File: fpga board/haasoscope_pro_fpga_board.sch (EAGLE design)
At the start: 406 parts, among them IC1 EP4CE30F23C6N, IC2 EPCQ16ASI8N, J1 2x5, SW1 SKQGADE010, SW2 SKQGADE010, U1 AMS1117-3.3, U2 AMS1117-2.5, U3 AMS1117-1.2, Y1 OSCILLATORSMD-5X3

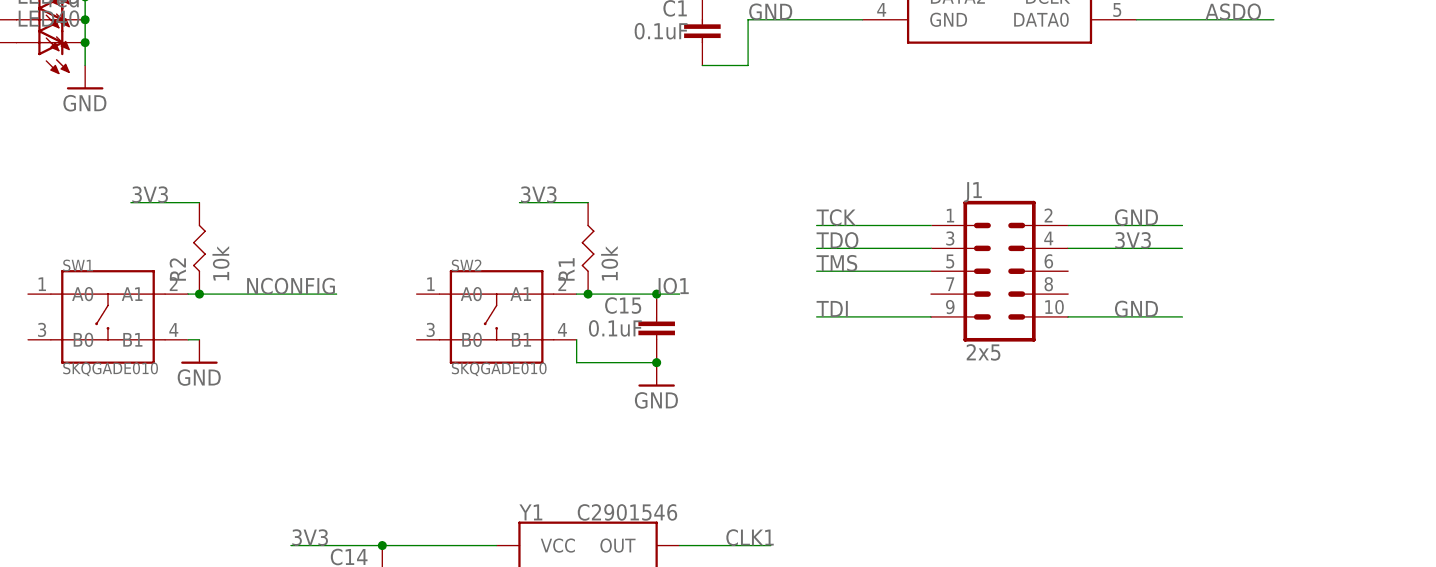
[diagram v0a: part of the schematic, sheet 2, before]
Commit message: pull tms and tdi up to 3v3
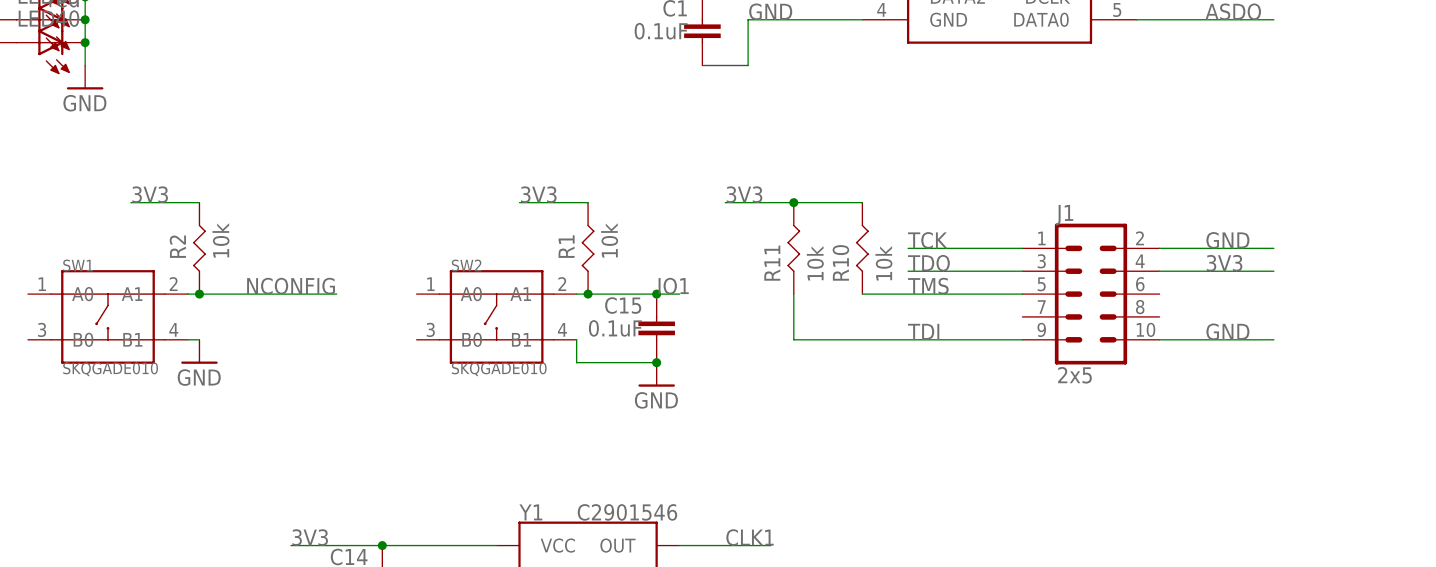
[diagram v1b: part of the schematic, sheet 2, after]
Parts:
- added R10, R11: 10k, FlashPCB_Resistors:RES-0402
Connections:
- net 3V3: now also R10.P$2, R11.P$2
- net TDI: now also R11.P$1
- net TMS: now also R10.P$1
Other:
- moved on the sheet: J1
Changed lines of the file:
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@@
 <part name="JP341" library="pinhead" library_urn="urn:adsk.eagle:library:325" deviceset="PINHD-1X1" device="" package3d_urn="urn:adsk.eagle:package:22485/2" value="1"/>
 <part name="JP342" library="pinhead" library_urn="urn:adsk.eagle:library:325" deviceset="PINHD-1X1" device="" package3d_urn="urn:adsk.eagle:package:22485/2" value="1"/>
+<part name="R10" library="FlashPCB_Resistors" deviceset="RES-0402" device="" value="10k"/>
+<part name="R11" library="FlashPCB_Resistors" deviceset="RES-0402" device="" value="10k"/>
 </parts>
 <sheets>
@@
 <attribute name="VALUE" x="92.456" y="197.739" size="1.778" layer="96" rot="R180"/>
 </instance>
-<instance part="J1" gate="G$1" x="127" y="170.18" smashed="yes">
-<attribute name="VALUE" x="123.19" y="160.274" size="1.778" layer="96" font="vector"/>
-<attribute name="NAME" x="123.19" y="178.308" size="1.778" layer="95" font="vector"/>
+<instance part="J1" gate="G$1" x="137.16" y="167.64" smashed="yes">
+<attribute name="VALUE" x="133.35" y="157.734" size="1.778" layer="96" font="vector"/>
+<attribute name="NAME" x="133.35" y="175.768" size="1.778" layer="95" font="vector"/>
 </instance>
 <instance part="C14" gate="C$1" x="58.42" y="134.62" smashed="yes" rot="R180">
@@
 </instance>
 <instance part="R1" gate="G$1" x="81.28" y="172.72" smashed="yes" rot="R90">
-<attribute name="NAME" x="79.7814" y="168.91" size="1.778" layer="95" rot="R90"/>
-<attribute name="VALUE" x="84.582" y="168.91" size="1.778" layer="96" rot="R90"/>
+<attribute name="NAME" x="79.7814" y="171.45" size="1.778" layer="95" rot="R90"/>
+<attribute name="VALUE" x="84.582" y="171.45" size="1.778" layer="96" rot="R90"/>
 </instance>
 <instance part="C15" gate="C$1" x="88.9" y="162.56" smashed="yes" rot="R180">
@@
 </instance>
 <instance part="R2" gate="G$1" x="38.1" y="172.72" smashed="yes" rot="R90">
-<attribute name="NAME" x="36.6014" y="168.91" size="1.778" layer="95" rot="R90"/>
-<attribute name="VALUE" x="41.402" y="168.91" size="1.778" layer="96" rot="R90"/>
+<attribute name="NAME" x="36.6014" y="171.45" size="1.778" layer="95" rot="R90"/>
+<attribute name="VALUE" x="41.402" y="171.45" size="1.778" layer="96" rot="R90"/>
 </instance>
 <instance part="R3" gate="G$1" x="7.62" y="170.18" smashed="yes" rot="R90">
@@
 <attribute name="VALUE" x="48.26" y="-10.16" size="1.778" layer="96"/>
 </instance>
+<instance part="R10" gate="G$1" x="111.76" y="172.72" smashed="yes" rot="R90">
+<attribute name="NAME" x="110.2614" y="168.91" size="1.778" layer="95" rot="R90"/>
+<attribute name="VALUE" x="115.062" y="168.91" size="1.778" layer="96" rot="R90"/>
+</instance>
+<instance part="R11" gate="G$1" x="104.14" y="172.72" smashed="yes" rot="R90">
+<attribute name="NAME" x="102.6414" y="168.91" size="1.778" layer="95" rot="R90"/>
+<attribute name="VALUE" x="107.442" y="168.91" size="1.778" layer="96" rot="R90"/>
+</instance>
 </instances>
 <busses>
@@
 <segment>
 <pinref part="J1" gate="G$1" pin="2"/>
-<wire x1="134.62" y1="175.26" x2="147.32" y2="175.26" width="0.1524" layer="91"/>
-<label x="139.7" y="175.26" size="1.778" layer="95"/>
+<wire x1="144.78" y1="172.72" x2="157.48" y2="172.72" width="0.1524" layer="91"/>
+<label x="149.86" y="172.72" size="1.778" layer="95"/>
 </segment>
 <segment>
 <pinref part="J1" gate="G$1" pin="10"/>
-<wire x1="134.62" y1="165.1" x2="147.32" y2="165.1" width="0.1524" layer="91"/>
-<label x="139.7" y="165.1" size="1.778" layer="95"/>
+<wire x1="144.78" y1="162.56" x2="157.48" y2="162.56" width="0.1524" layer="91"/>
+<label x="149.86" y="162.56" size="1.778" layer="95"/>
 </segment>
 <segment>
@@
 <segment>
 <pinref part="J1" gate="G$1" pin="4"/>
-<wire x1="134.62" y1="172.72" x2="147.32" y2="172.72" width="0.1524" layer="91"/>
-<label x="139.7" y="172.72" size="1.778" layer="95"/>
+<wire x1="144.78" y1="170.18" x2="157.48" y2="170.18" width="0.1524" layer="91"/>
+<label x="149.86" y="170.18" size="1.778" layer="95"/>
 </segment>
 <segment>
@@
 <label x="111.76" y="101.6" size="1.778" layer="95"/>
 </segment>
+<segment>
+<pinref part="R10" gate="G$1" pin="P$2"/>
+<wire x1="111.76" y1="177.8" x2="104.14" y2="177.8" width="0.1524" layer="91"/>
+<pinref part="R11" gate="G$1" pin="P$2"/>
+<junction x="104.14" y="177.8"/>
+<label x="96.52" y="177.8" size="1.778" layer="95"/>
+<wire x1="96.52" y1="177.8" x2="104.14" y2="177.8" width="0.1524" layer="91"/>
+</segment>
 </net>
 <net name="N$33" class="0">
@@
 <segment>
 <pinref part="J1" gate="G$1" pin="5"/>
-<wire x1="119.38" y1="170.18" x2="106.68" y2="170.18" width="0.1524" layer="91"/>
-<label x="106.68" y="170.18" size="1.778" layer="95"/>
+<wire x1="129.54" y1="167.64" x2="111.76" y2="167.64" width="0.1524" layer="91"/>
+<label x="116.84" y="167.64" size="1.778" layer="95"/>
+<pinref part="R10" gate="G$1" pin="P$1"/>
 </segment>
 </net>
@@
 <segment>
 <pinref part="J1" gate="G$1" pin="1"/>
-<wire x1="119.38" y1="175.26" x2="106.68" y2="175.26" width="0.1524" layer="91"/>
-<label x="106.68" y="175.26" size="1.778" layer="95"/>
+<wire x1="129.54" y1="172.72" x2="116.84" y2="172.72" width="0.1524" layer="91"/>
+<label x="116.84" y="172.72" size="1.778" layer="95"/>
 </segment>
 </net>
@@
 <segment>
 <pinref part="J1" gate="G$1" pin="3"/>
-<wire x1="119.38" y1="172.72" x2="106.68" y2="172.72" width="0.1524" layer="91"/>
-<label x="106.68" y="172.72" size="1.778" layer="95"/>
+<wire x1="129.54" y1="170.18" x2="116.84" y2="170.18" width="0.1524" layer="91"/>
+<label x="116.84" y="170.18" size="1.778" layer="95"/>
 </segment>
 </net>
@@
 <segment>
 <pinref part="J1" gate="G$1" pin="9"/>
-<wire x1="119.38" y1="165.1" x2="106.68" y2="165.1" width="0.1524" layer="91"/>
-<label x="106.68" y="165.1" size="1.778" layer="95"/>
+<label x="116.84" y="162.56" size="1.778" layer="95"/>
+<pinref part="R11" gate="G$1" pin="P$1"/>
+<wire x1="104.14" y1="167.64" x2="104.14" y2="162.56" width="0.1524" layer="91"/>
+<wire x1="104.14" y1="162.56" x2="129.54" y2="162.56" width="0.1524" layer="91"/>
 </segment>
 </net>

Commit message: pull down tck to gnd with 1k
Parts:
- added R12: 1k, FlashPCB_Resistors:RES-0402
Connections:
- net GND: now also R12.P$1
- net TCK: now also R12.P$2
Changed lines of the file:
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@@
 <part name="R10" library="FlashPCB_Resistors" deviceset="RES-0402" device="" value="10k"/>
 <part name="R11" library="FlashPCB_Resistors" deviceset="RES-0402" device="" value="10k"/>
+<part name="R12" library="FlashPCB_Resistors" deviceset="RES-0402" device="" value="1k"/>
 </parts>
 <sheets>
@@
 <attribute name="VALUE" x="107.442" y="168.91" size="1.778" layer="96" rot="R90"/>
 </instance>
+<instance part="R12" gate="G$1" x="137.16" y="180.34" smashed="yes" rot="R180">
+<attribute name="NAME" x="140.97" y="178.8414" size="1.778" layer="95" rot="R180"/>
+<attribute name="VALUE" x="140.97" y="183.642" size="1.778" layer="96" rot="R180"/>
+</instance>
 </instances>
 <busses>
@@
 <segment>
 <pinref part="J1" gate="G$1" pin="2"/>
-<wire x1="144.78" y1="172.72" x2="157.48" y2="172.72" width="0.1524" layer="91"/>
+<wire x1="144.78" y1="172.72" x2="147.32" y2="172.72" width="0.1524" layer="91"/>
 <label x="149.86" y="172.72" size="1.778" layer="95"/>
+<pinref part="R12" gate="G$1" pin="P$1"/>
+<wire x1="147.32" y1="172.72" x2="157.48" y2="172.72" width="0.1524" layer="91"/>
+<wire x1="142.24" y1="180.34" x2="147.32" y2="180.34" width="0.1524" layer="91"/>
+<wire x1="147.32" y1="180.34" x2="147.32" y2="172.72" width="0.1524" layer="91"/>
+<junction x="147.32" y="172.72"/>
 </segment>
 <segment>
@@
 <segment>
 <pinref part="J1" gate="G$1" pin="1"/>
-<wire x1="129.54" y1="172.72" x2="116.84" y2="172.72" width="0.1524" layer="91"/>
+<wire x1="129.54" y1="172.72" x2="124.46" y2="172.72" width="0.1524" layer="91"/>
 <label x="116.84" y="172.72" size="1.778" layer="95"/>
+<pinref part="R12" gate="G$1" pin="P$2"/>
+<wire x1="124.46" y1="172.72" x2="116.84" y2="172.72" width="0.1524" layer="91"/>
+<wire x1="132.08" y1="180.34" x2="124.46" y2="180.34" width="0.1524" layer="91"/>
+<wire x1="124.46" y1="180.34" x2="124.46" y2="172.72" width="0.1524" layer="91"/>
+<junction x="124.46" y="172.72"/>
 </segment>
 </net>
